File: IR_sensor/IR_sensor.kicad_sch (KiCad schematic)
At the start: 0 parts

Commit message: added schematic of IR_sensor
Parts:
- added CR1: GREEN LED, TLL_Series_VIS, symbol IR_sensor_lib:TLLG4401
- added CR2: IR LED, TLL_Series_VIS, symbol IR_sensor_lib:TLLG4401
- added J1: Signal_out, symbol Connector:Conn_01x01_Pin
- added J2: 5V_In, symbol Connector:Conn_01x01_Pin
- added J3: GND, symbol Connector:Conn_01x01_Pin
- added Q1: BPV11F, BPV11F:XDCR_BPV11F, symbol IR_sensor_lib:BPV11F
- added R1: 10k Ohm, symbol Device:R
- added R2: 330 Ohm, symbol Device:R
- added R3: 1M Ohm, symbol Device:R
- added R4: 100 Ohm, symbol Device:R
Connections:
- new net: Q1.B, R3.1
- new net: CR1.2, J1.1 (Pin_1), Q1.C, R1.2
- new net: CR2.2, R4.2
- new net: J2.1 (Pin_1), R1.1, R4.1
- new net: CR1.1, R2.1
- new net GND: CR2.1, J3.1 (Pin_1), Q1.E, R2.2, R3.2

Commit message: Added new PCB design
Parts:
- CR1: footprint TLL_Series_VIS -> IR_sensor_lib:TLL_Series_LED_GR
- CR2: footprint TLL_Series_VIS -> LED_THT:LED_D5.0mm_IRGrey
- J1, J2, J3: footprint (none) -> Connector_PinHeader_2.54mm:PinHeader_1x01_P2.54mm_Vertical
- Q1: footprint BPV11F:XDCR_BPV11F -> IR_sensor_lib:Phototransistor
- R1, R2, R3, R4: footprint (none) -> Resistor_THT:R_Axial_DIN0207_L6.3mm_D2.5mm_P5.08mm_Vertical
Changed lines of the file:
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@@
 			)
 		)
-		(property "Footprint" "BPV11F:XDCR_BPV11F"
+		(property "Footprint" "IR_sensor_lib:Phototransistor"
 			(at 145.796 82.296 0)
 			(effects
@@
 			)
 		)
-		(property "Footprint" ""
+		(property "Footprint" "Connector_PinHeader_2.54mm:PinHeader_1x01_P2.54mm_Vertical"
 			(at 212.09 63.5 0)
 			(effects
@@
 			)
 		)
-		(property "Footprint" "TLL_Series_VIS"
+		(property "Footprint" "LED_THT:LED_D5.0mm_IRGrey"
 			(at 88.138 63.246 0)
 			(effects
@@
 			)
 		)
-		(property "Footprint" ""
+		(property "Footprint" "Resistor_THT:R_Axial_DIN0207_L6.3mm_D2.5mm_P5.08mm_Vertical"
 			(at 137.922 91.44 90)
 			(effects
@@
 			)
 		)
-		(property "Footprint" ""
+		(property "Footprint" "Resistor_THT:R_Axial_DIN0207_L6.3mm_D2.5mm_P5.08mm_Vertical"
 			(at 156.972 53.34 90)
 			(effects
@@
 			)
 		)
-		(property "Footprint" ""
+		(property "Footprint" "Resistor_THT:R_Axial_DIN0207_L6.3mm_D2.5mm_P5.08mm_Vertical"
 			(at 88.392 60.96 90)
 			(effects
@@
 			)
 		)
-		(property "Footprint" "TLL_Series_VIS"
+		(property "Footprint" "IR_sensor_lib:TLL_Series_LED_GR"
 			(at 197.358 65.786 0)
 			(effects
@@
 			)
 		)
-		(property "Footprint" ""
+		(property "Footprint" "Connector_PinHeader_2.54mm:PinHeader_1x01_P2.54mm_Vertical"
 			(at 153.67 115.57 0)
 			(effects
@@
 			)
 		)
-		(property "Footprint" ""
+		(property "Footprint" "Connector_PinHeader_2.54mm:PinHeader_1x01_P2.54mm_Vertical"
 			(at 158.75 36.83 0)
 			(effects
@@
 			)
 		)
-		(property "Footprint" ""
+		(property "Footprint" "Resistor_THT:R_Axial_DIN0207_L6.3mm_D2.5mm_P5.08mm_Vertical"
 			(at 197.612 90.17 90)
 			(effects

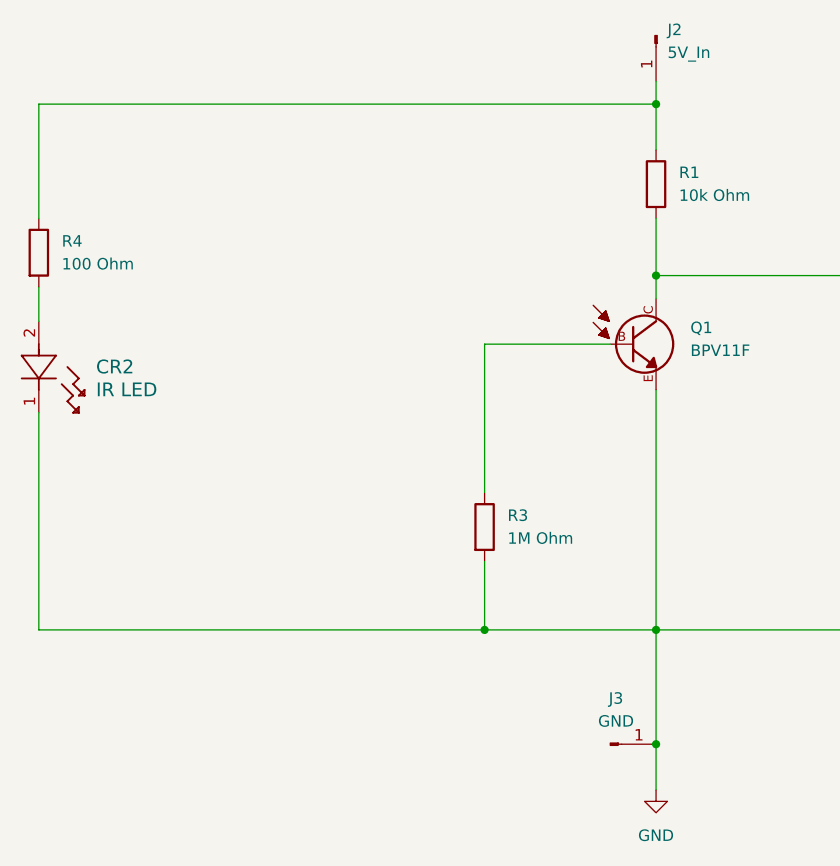
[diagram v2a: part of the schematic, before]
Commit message: Divided transmitter and reciever
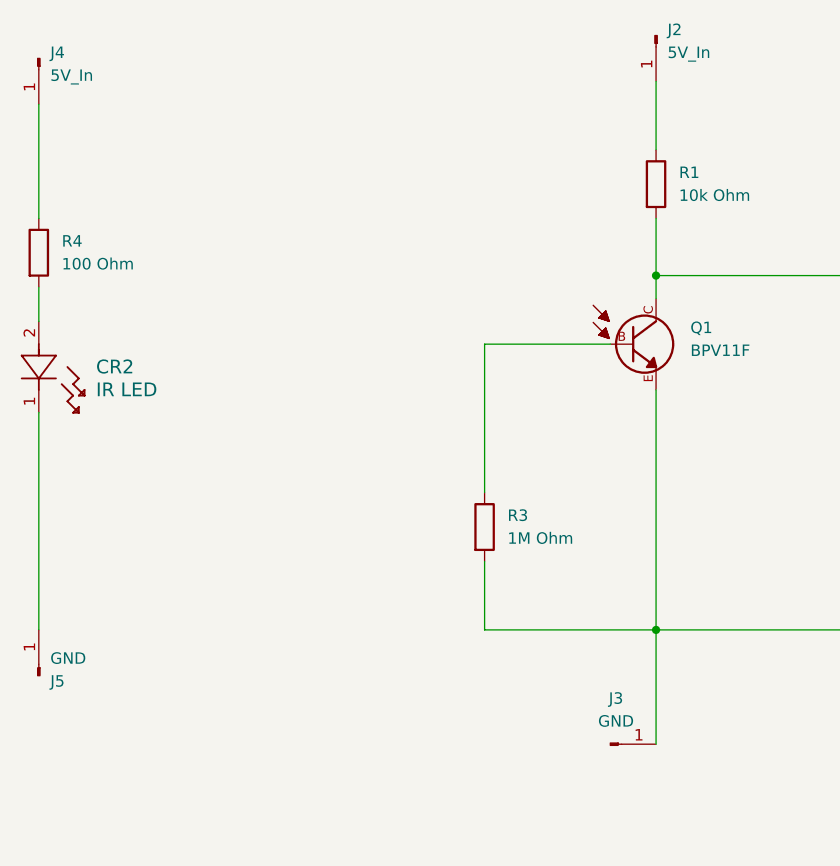
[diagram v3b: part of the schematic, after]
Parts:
- added J4: 5V_In, Connector_PinHeader_2.54mm:PinHeader_1x01_P2.54mm_Vertical, symbol Connector:Conn_01x01_Pin
- added J5: GND, Connector_PinHeader_2.54mm:PinHeader_1x01_P2.54mm_Vertical, symbol Connector:Conn_01x01_Pin
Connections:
- net at J2.1 (Pin_1), R1.1: no longer R4.1
- net GND: no longer names the net of J3.1 (Pin_1), Q1.E, R2.2, R3.2
- net GND: no longer CR2.1
- new net: CR2.1, J5.1 (Pin_1)
- new net: J4.1 (Pin_1), R4.1
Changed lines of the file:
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@@
-	)
-	(junction
-		(at 158.75 44.45)
-		(diameter 0)
-		(color 0 0 0 0)
-	)
-	(junction
-		(at 158.75 115.57)
-		(diameter 0)
-		(color 0 0 0 0)
 	)
 	(junction
@@
 	)
 	(junction
-		(at 139.7 102.87)
-		(diameter 0)
-		(color 0 0 0 0)
-	)
-	(junction
 		(at 158.75 63.5)
 		(diameter 0)
@@
 	(wire
 		(pts
-			(xy 158.75 41.91) (xy 158.75 44.45)
+			(xy 158.75 41.91) (xy 158.75 49.53)
 		)
 		(stroke
@@
 	(wire
 		(pts
-			(xy 158.75 115.57) (xy 158.75 120.65)
-		)
-		(stroke
-			(width 0)
-			(type default)
-		)
-	)
-	(wire
-		(pts
 			(xy 158.75 102.87) (xy 158.75 115.57)
 		)
@@
 	(wire
 		(pts
-			(xy 90.17 44.45) (xy 158.75 44.45)
-		)
-		(stroke
-			(width 0)
-			(type default)
-		)
-	)
-	(wire
-		(pts
 			(xy 158.75 63.5) (xy 199.39 63.5)
 		)
@@
 	(wire
 		(pts
-			(xy 90.17 102.87) (xy 139.7 102.87)
-		)
-		(stroke
-			(width 0)
-			(type default)
-		)
-	)
-	(wire
-		(pts
 			(xy 158.75 57.15) (xy 158.75 63.5)
 		)
@@
 		(pts
 			(xy 153.67 71.12) (xy 139.7 71.12)
-		)
-		(stroke
-			(width 0)
-			(type default)
-		)
-	)
-	(wire
-		(pts
-			(xy 158.75 44.45) (xy 158.75 49.53)
 		)
 		(stroke
@@
 	(symbol
 		(lib_id "Connector:Conn_01x01_Pin")
+		(at 90.17 107.95 270)
+		(mirror x)
+		(unit 1)
+		(exclude_from_sim no)
+		(in_bom yes)
+		(on_board yes)
+		(dnp no)
+		(property "Reference" "J5"
+			(at 91.44 108.5851 90)
+			(effects
+				(font
+					(size 1.27 1.27)
+				)
+				(justify left)
+			)
+		)
+		(property "Value" "GND"
+			(at 91.44 106.0451 90)
+			(effects
+				(font
+					(size 1.27 1.27)
+				)
+				(justify left)
+			)
+		)
+		(property "Footprint" "Connector_PinHeader_2.54mm:PinHeader_1x01_P2.54mm_Vertical"
+			(at 90.17 107.95 0)
+			(effects
+				(font
+					(size 1.27 1.27)
+				)
+				(hide yes)
+			)
+		)
+		(property "Datasheet" "~"
+			(at 90.17 107.95 0)
+			(effects
+				(font
+					(size 1.27 1.27)
+				)
+				(hide yes)
+			)
+		)
+		(property "Description" "Generic connector, single row, 01x01, script generated"
+			(at 90.17 107.95 0)
+			(effects
+				(font
+					(size 1.27 1.27)
+				)
+				(hide yes)
+			)
+		)
+		(pin "1"
+		)
+		(instances
+			(project "IR_sensor"
+				(path "/d6ceb58d-433d-4683-8247-0a402c7551db"
+					(reference "J5")
+					(unit 1)
+				)
+			)
+		)
+	)
+	(symbol
+		(lib_id "Connector:Conn_01x01_Pin")
 		(at 212.09 63.5 0)
 		(mirror y)
@@
 	)
 	(symbol
-		(lib_id "power:GND")
-		(at 158.75 120.65 0)
+		(lib_id "Connector:Conn_01x01_Pin")
+		(at 90.17 39.37 270)
 		(unit 1)
 		(exclude_from_sim no)
@@
 		(dnp no)
 		(fields_autoplaced yes)
-		(property "Reference" "#PWR01"
-			(at 158.75 127 0)
-			(effects
-				(font
-					(size 1.27 1.27)
-				)
-				(hide yes)
-			)
-		)
-		(property "Value" "GND"
-			(at 158.75 125.73 0)
-			(effects
-				(font
-					(size 1.27 1.27)
-				)
-			)
-		)
-		(property "Footprint" ""
-			(at 158.75 120.65 0)
-			(effects
-				(font
-					(size 1.27 1.27)
-				)
-				(hide yes)
-			)
-		)
-		(property "Datasheet" ""
-			(at 158.75 120.65 0)
-			(effects
-				(font
-					(size 1.27 1.27)
-				)
-				(hide yes)
-			)
-		)
-		(property "Description" "Power symbol creates a global label with name \"GND\" , ground"
-			(at 158.75 120.65 0)
+		(property "Reference" "J4"
+			(at 91.44 38.7349 90)
+			(effects
+				(font
+					(size 1.27 1.27)
+				)
+				(justify left)
+			)
+		)
+		(property "Value" "5V_In"
+			(at 91.44 41.2749 90)
+			(effects
+				(font
+					(size 1.27 1.27)
+				)
+				(justify left)
+			)
+		)
+		(property "Footprint" "Connector_PinHeader_2.54mm:PinHeader_1x01_P2.54mm_Vertical"
+			(at 90.17 39.37 0)
+			(effects
+				(font
+					(size 1.27 1.27)
+				)
+				(hide yes)
+			)
+		)
+		(property "Datasheet" "~"
+			(at 90.17 39.37 0)
+			(effects
+				(font
+					(size 1.27 1.27)
+				)
+				(hide yes)
+			)
+		)
+		(property "Description" "Generic connector, single row, 01x01, script generated"
+			(at 90.17 39.37 0)
 			(effects
 				(font
@@
 		)
 		(instances
-			(project ""
+			(project "IR_sensor"
 				(path "/d6ceb58d-433d-4683-8247-0a402c7551db"
-					(reference "#PWR01")
+					(reference "J4")
 					(unit 1)
 				)

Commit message: Added new component
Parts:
- removed R3: 1M Ohm, Resistor_THT:R_Axial_DIN0207_L6.3mm_D2.5mm_P5.08mm_Vertical, symbol Device:R
- added U1: LM311P, IR_sensor_lib:Voltage_comparator, symbol IR_sensor_lib:LM311P
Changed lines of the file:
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@@
-	(wire
-		(pts
-			(xy 139.7 102.87) (xy 158.75 102.87)
-		)
-		(stroke
-			(width 0)
-			(type default)
-		)
-	)
-	(wire
-		(pts
-			(xy 139.7 95.25) (xy 139.7 102.87)
-		)
-		(stroke
-			(width 0)
-			(type default)
-		)
-	)
 	(wire
 		(pts
@@
 	(wire
 		(pts
-			(xy 139.7 71.12) (xy 139.7 87.63)
-		)
-		(stroke
-			(width 0)
-			(type default)
-		)
-	)
-	(wire
-		(pts
 			(xy 90.17 78.74) (xy 90.17 102.87)
 		)
@@
 		(pts
 			(xy 199.39 102.87) (xy 158.75 102.87)
-		)
-		(stroke
-			(width 0)
-			(type default)
-		)
-	)
-	(wire
-		(pts
-			(xy 153.67 71.12) (xy 139.7 71.12)
 		)
 		(stroke
@@
 	)
 	(symbol
-		(lib_name "R_1")
-		(lib_id "Device:R")
-		(at 139.7 91.44 0)
+		(lib_id "IR_sensor_lib:LM311P")
+		(at 234.95 66.04 0)
 		(unit 1)
 		(exclude_from_sim no)
@@
 		(dnp no)
 		(fields_autoplaced yes)
-		(property "Reference" "R3"
-			(at 142.24 90.1699 0)
-			(effects
-				(font
-					(size 1.27 1.27)
-				)
-				(justify left)
-			)
-		)
-		(property "Value" "1M Ohm"
-			(at 142.24 92.7099 0)
-			(effects
-				(font
-					(size 1.27 1.27)
-				)
-				(justify left)
-			)
-		)
-		(property "Footprint" "Resistor_THT:R_Axial_DIN0207_L6.3mm_D2.5mm_P5.08mm_Vertical"
-			(at 137.922 91.44 90)
-			(effects
-				(font
-					(size 1.27 1.27)
-				)
-				(hide yes)
-			)
-		)
-		(property "Datasheet" "~"
-			(at 139.7 91.44 0)
-			(effects
-				(font
-					(size 1.27 1.27)
-				)
-				(hide yes)
-			)
-		)
-		(property "Description" "Resistor"
-			(at 139.7 91.44 0)
-			(effects
-				(font
-					(size 1.27 1.27)
-				)
-				(hide yes)
-			)
+		(property "Reference" "U1"
+			(at 235.585 53.34 0)
+			(effects
+				(font
+					(size 1.524 1.524)
+				)
+			)
+		)
+		(property "Value" "LM311P"
+			(at 235.585 55.88 0)
+			(effects
+				(font
+					(size 1.524 1.524)
+				)
+			)
+		)
+		(property "Footprint" "IR_sensor_lib:Voltage_comparator"
+			(at 226.06 77.724 0)
+			(effects
+				(font
+					(size 1.27 1.27)
+					(italic yes)
+				)
+				(hide yes)
+			)
+		)
+		(property "Datasheet" "LM311P"
+			(at 228.346 79.756 0)
+			(effects
+				(font
+					(size 1.27 1.27)
+					(italic yes)
+				)
+				(hide yes)
+			)
+		)
+		(property "Description" ""
+			(at 234.95 66.04 0)
+			(effects
+				(font
+					(size 1.27 1.27)
+				)
+				(hide yes)
+			)
+		)
+		(pin "2"
 		)
 		(pin "1"
 		)
-		(pin "2"
+		(pin "7"
+		)
+		(pin "8"
+		)
+		(pin "6"
+		)
+		(pin "5"
+		)
+		(pin "3"
+		)
+		(pin "4"
 		)
 		(instances
 			(project ""
 				(path "/d6ceb58d-433d-4683-8247-0a402c7551db"
-					(reference "R3")
+					(reference "U1")
 					(unit 1)
 				)

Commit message: Finalized PCB design
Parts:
- added R3: 3k, Resistor_THT:R_Axial_DIN0204_L3.6mm_D1.6mm_P5.08mm_Horizontal, symbol Device:R
- added R5: 2.2k, Resistor_THT:R_Axial_DIN0204_L3.6mm_D1.6mm_P5.08mm_Horizontal, symbol Device:R
- added R6: 500, Resistor_THT:R_Axial_DIN0204_L3.6mm_D1.6mm_P5.08mm_Horizontal, symbol Device:R
- R1, R2, R4: footprint Resistor_THT:R_Axial_DIN0207_L6.3mm_D2.5mm_P5.08mm_Vertical -> Resistor_THT:R_Axial_DIN0204_L3.6mm_D1.6mm_P5.08mm_Horizontal
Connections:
- net at CR1.2, Q1.C, R1.2: now also U1.3 (IN-); no longer J1.1 (Pin_1)
- net GND: now reaches J3.1 (Pin_1), Q1.E, R2.2
- net GND: now also U1.1 (EMITOUT), U1.4 (VCC-), R5.2
- net at U1.2 (IN+): now also R3.2, R5.1
- net +5V: now reaches U1.5 (BALANCE)
- net +5V: now also J2.1 (Pin_1), R1.1, U1.8 (VCC+), R3.1, R6.1
- net at U1.7 (COLOUT): now also J1.1 (Pin_1), R6.2
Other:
- moved on the sheet: CR1, CR2, J1, J2, J3, J4, J5, Q1, R1, R2, R4, U1

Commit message: Changed pcb design, added voltage division on output
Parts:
- added R7: 10k, Resistor_THT:R_Axial_DIN0204_L3.6mm_D1.6mm_P5.08mm_Horizontal, symbol Device:R
- R6: value 500 -> 10k
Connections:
- net GND: now also R7.2
- net at J1.1 (Pin_1), R6.2, U1.7 (COLOUT): now also R7.1
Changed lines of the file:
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@@
+	(wire
+		(pts
+			(xy 224.79 74.93) (xy 224.79 85.09)
+		)
+		(stroke
+			(width 0)
+			(type default)
+		)
+	)
 	(wire
 		(pts
@@
 		(pts
 			(xy 137.16 101.6) (xy 137.16 110.49)
+		)
+		(stroke
+			(width 0)
+			(type default)
+		)
+	)
+	(wire
+		(pts
+			(xy 224.79 92.71) (xy 224.79 97.79)
 		)
 		(stroke
@@
 				(path "/d6ceb58d-433d-4683-8247-0a402c7551db"
 					(reference "#PWR06")
+					(unit 1)
+				)
+			)
+		)
+	)
+	(symbol
+		(lib_id "power:GND")
+		(at 224.79 97.79 0)
+		(unit 1)
+		(exclude_from_sim no)
+		(in_bom yes)
+		(on_board yes)
+		(dnp no)
+		(fields_autoplaced yes)
+		(property "Reference" "#PWR010"
+			(at 224.79 104.14 0)
+			(effects
+				(font
+					(size 1.27 1.27)
+				)
+				(hide yes)
+			)
+		)
+		(property "Value" "GND"
+			(at 224.79 102.87 0)
+			(effects
+				(font
+					(size 1.27 1.27)
+				)
+			)
+		)
+		(property "Footprint" ""
+			(at 224.79 97.79 0)
+			(effects
+				(font
+					(size 1.27 1.27)
+				)
+				(hide yes)
+			)
+		)
+		(property "Datasheet" ""
+			(at 224.79 97.79 0)
+			(effects
+				(font
+					(size 1.27 1.27)
+				)
+				(hide yes)
+			)
+		)
+		(property "Description" "Power symbol creates a global label with name \"GND\" , ground"
+			(at 224.79 97.79 0)
+			(effects
+				(font
+					(size 1.27 1.27)
+				)
+				(hide yes)
+			)
+		)
+		(pin "1"
+		)
+		(instances
+			(project ""
+				(path "/d6ceb58d-433d-4683-8247-0a402c7551db"
+					(reference "#PWR010")
+					(unit 1)
+				)
+			)
+		)
+	)
+	(symbol
+		(lib_name "R_4")
+		(lib_id "Device:R")
+		(at 224.79 88.9 0)
+		(unit 1)
+		(exclude_from_sim no)
+		(in_bom yes)
+		(on_board yes)
+		(dnp no)
+		(fields_autoplaced yes)
+		(property "Reference" "R7"
+			(at 227.33 87.6299 0)
+			(effects
+				(font
+					(size 1.27 1.27)
+				)
+				(justify left)
+			)
+		)
+		(property "Value" "10k"
+			(at 227.33 90.1699 0)
+			(effects
+				(font
+					(size 1.27 1.27)
+				)
+				(justify left)
+			)
+		)
+		(property "Footprint" "Resistor_THT:R_Axial_DIN0204_L3.6mm_D1.6mm_P5.08mm_Horizontal"
+			(at 223.012 88.9 90)
+			(effects
+				(font
+					(size 1.27 1.27)
+				)
+				(hide yes)
+			)
+		)
+		(property "Datasheet" "~"
+			(at 224.79 88.9 0)
+			(effects
+				(font
+					(size 1.27 1.27)
+				)
+				(hide yes)
+			)
+		)
+		(property "Description" "Resistor"
+			(at 224.79 88.9 0)
+			(effects
+				(font
+					(size 1.27 1.27)
+				)
+				(hide yes)
+			)
+		)
+		(pin "1"
+		)
+		(pin "2"
+		)
+		(instances
+			(project "IR_sensor"
+				(path "/d6ceb58d-433d-4683-8247-0a402c7551db"
+					(reference "R7")
 					(unit 1)
 				)
@@
 			)
 		)
-		(property "Value" "500"
+		(property "Value" "10k"
 			(at 227.33 63.4999 0)
 			(effects

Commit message: Updated resistor values
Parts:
- R6: value 10k -> 570
- R7: value 10k -> 1k
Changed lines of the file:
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@@
 			)
 		)
-		(property "Value" "10k"
+		(property "Value" "1k"
 			(at 227.33 90.1699 0)
 			(effects
@@
 			)
 		)
-		(property "Value" "10k"
+		(property "Value" "570"
 			(at 227.33 63.4999 0)
 			(effects
